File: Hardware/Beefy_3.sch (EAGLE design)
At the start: 21 parts, among them J1 USB-MINIB-5PIN, U1 3.3V, U2 FT232RL-BASICSSOP

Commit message: Added PROD_IDs to library parts and updated them
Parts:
- JP1: device SparkFun:M06SMD-FEMALE-V2 -> SparkFun-Connectors:M06SMD-FEMALE-V2
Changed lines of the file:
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@@
 <grid distance="0.1" unitdist="inch" unit="inch" style="lines" multiple="1" display="no" altdistance="0.01" altunitdist="inch" altunit="inch"/>
 <layers>
-<layer number="1" name="Top" color="4" fill="1" visible="yes" active="no"/>
-<layer number="2" name="Route2" color="1" fill="3" visible="yes" active="no"/>
-<layer number="3" name="Route3" color="4" fill="3" visible="yes" active="no"/>
-<layer number="4" name="Route4" color="1" fill="4" visible="yes" active="no"/>
-<layer number="5" name="Route5" color="4" fill="4" visible="yes" active="no"/>
-<layer number="6" name="Route6" color="1" fill="8" visible="yes" active="no"/>
-<layer number="7" name="Route7" color="4" fill="8" visible="yes" active="no"/>
-<layer number="8" name="Route8" color="1" fill="2" visible="yes" active="no"/>
-<layer number="9" name="Route9" color="4" fill="2" visible="yes" active="no"/>
-<layer number="10" name="Route10" color="1" fill="7" visible="yes" active="no"/>
-<layer number="11" name="Route11" color="4" fill="7" visible="yes" active="no"/>
-<layer number="12" name="Route12" color="1" fill="5" visible="yes" active="no"/>
-<layer number="13" name="Route13" color="4" fill="5" visible="yes" active="no"/>
-<layer number="14" name="Route14" color="1" fill="6" visible="yes" active="no"/>
-<layer number="15" name="Route15" color="4" fill="6" visible="yes" active="no"/>
-<layer number="16" name="Bottom" color="1" fill="1" visible="yes" active="no"/>
-<layer number="17" name="Pads" color="2" fill="1" visible="yes" active="no"/>
-<layer number="18" name="Vias" color="2" fill="1" visible="yes" active="no"/>
-<layer number="19" name="Unrouted" color="6" fill="1" visible="yes" active="no"/>
-<layer number="20" name="Dimension" color="15" fill="1" visible="yes" active="no"/>
-<layer number="21" name="tPlace" color="16" fill="1" visible="yes" active="no"/>
-<layer number="22" name="bPlace" color="14" fill="1" visible="yes" active="no"/>
-<layer number="23" name="tOrigins" color="15" fill="1" visible="yes" active="no"/>
-<layer number="24" name="bOrigins" color="15" fill="1" visible="yes" active="no"/>
-<layer number="25" name="tNames" color="7" fill="1" visible="yes" active="no"/>
-<layer number="26" name="bNames" color="7" fill="1" visible="yes" active="no"/>
-<layer number="27" name="tValues" color="7" fill="1" visible="yes" active="no"/>
-<layer number="28" name="bValues" color="7" fill="1" visible="yes" active="no"/>
+<layer number="1" name="Top" color="4" fill="1" visible="no" active="no"/>
+<layer number="2" name="Route2" color="1" fill="3" visible="no" active="no"/>
+<layer number="3" name="Route3" color="4" fill="3" visible="no" active="no"/>
+<layer number="4" name="Route4" color="1" fill="4" visible="no" active="no"/>
+<layer number="5" name="Route5" color="4" fill="4" visible="no" active="no"/>
+<layer number="6" name="Route6" color="1" fill="8" visible="no" active="no"/>
+<layer number="7" name="Route7" color="4" fill="8" visible="no" active="no"/>
+<layer number="8" name="Route8" color="1" fill="2" visible="no" active="no"/>
+<layer number="9" name="Route9" color="4" fill="2" visible="no" active="no"/>
+<layer number="10" name="Route10" color="1" fill="7" visible="no" active="no"/>
+<layer number="11" name="Route11" color="4" fill="7" visible="no" active="no"/>
+<layer number="12" name="Route12" color="1" fill="5" visible="no" active="no"/>
+<layer number="13" name="Route13" color="4" fill="5" visible="no" active="no"/>
+<layer number="14" name="Route14" color="1" fill="6" visible="no" active="no"/>
+<layer number="15" name="Route15" color="4" fill="6" visible="no" active="no"/>
+<layer number="16" name="Bottom" color="1" fill="1" visible="no" active="no"/>
+<layer number="17" name="Pads" color="2" fill="1" visible="no" active="no"/>
+<layer number="18" name="Vias" color="2" fill="1" visible="no" active="no"/>
+<layer number="19" name="Unrouted" color="6" fill="1" visible="no" active="no"/>
+<layer number="20" name="Dimension" color="15" fill="1" visible="no" active="no"/>
+<layer number="21" name="tPlace" color="16" fill="1" visible="no" active="no"/>
+<layer number="22" name="bPlace" color="14" fill="1" visible="no" active="no"/>
+<layer number="23" name="tOrigins" color="15" fill="1" visible="no" active="no"/>
+<layer number="24" name="bOrigins" color="15" fill="1" visible="no" active="no"/>
+<layer number="25" name="tNames" color="7" fill="1" visible="no" active="no"/>
+<layer number="26" name="bNames" color="7" fill="1" visible="no" active="no"/>
+<layer number="27" name="tValues" color="7" fill="1" visible="no" active="no"/>
+<layer number="28" name="bValues" color="7" fill="1" visible="no" active="no"/>
 <layer number="29" name="tStop" color="7" fill="3" visible="no" active="no"/>
 <layer number="30" name="bStop" color="7" fill="6" visible="no" active="no"/>
@@
 <layer number="35" name="tGlue" color="7" fill="4" visible="no" active="no"/>
 <layer number="36" name="bGlue" color="7" fill="5" visible="no" active="no"/>
-<layer number="37" name="tTest" color="7" fill="1" visible="yes" active="no"/>
-<layer number="38" name="bTest" color="7" fill="1" visible="yes" active="no"/>
+<layer number="37" name="tTest" color="7" fill="1" visible="no" active="no"/>
+<layer number="38" name="bTest" color="7" fill="1" visible="no" active="no"/>
 <layer number="39" name="tKeepout" color="4" fill="11" visible="no" active="no"/>
 <layer number="40" name="bKeepout" color="1" fill="11" visible="no" active="no"/>
@@
 <layer number="44" name="Drills" color="7" fill="1" visible="no" active="no"/>
 <layer number="45" name="Holes" color="7" fill="1" visible="no" active="no"/>
-<layer number="46" name="Milling" color="3" fill="1" visible="yes" active="no"/>
-<layer number="47" name="Measures" color="7" fill="1" visible="yes" active="no"/>
-<layer number="48" name="Document" color="7" fill="1" visible="yes" active="no"/>
-<layer number="49" name="Reference" color="7" fill="1" visible="yes" active="no"/>
-<layer number="50" name="dxf" color="7" fill="1" visible="yes" active="no"/>
-<layer number="51" name="tDocu" color="6" fill="1" visible="yes" active="no"/>
-<layer number="52" name="bDocu" color="7" fill="1" visible="yes" active="no"/>
-<layer number="53" name="tGND_GNDA" color="7" fill="9" visible="yes" active="no"/>
-<layer number="54" name="bGND_GNDA" color="1" fill="9" visible="yes" active="no"/>
-<layer number="56" name="wert" color="7" fill="1" visible="yes" active="no"/>
-<layer number="57" name="tCAD" color="7" fill="1" visible="yes" active="no"/>
-<layer number="59" name="tCarbon" color="7" fill="1" visible="yes" active="no"/>
-<layer number="60" name="bCarbon" color="7" fill="1" visible="yes" active="no"/>
+<layer number="46" name="Milling" color="3" fill="1" visible="no" active="no"/>
+<layer number="47" name="Measures" color="7" fill="1" visible="no" active="no"/>
+<layer number="48" name="Document" color="7" fill="1" visible="no" active="no"/>
+<layer number="49" name="Reference" color="7" fill="1" visible="no" active="no"/>
+<layer number="50" name="dxf" color="7" fill="1" visible="no" active="no"/>
+<layer number="51" name="tDocu" color="6" fill="1" visible="no" active="no"/>
+<layer number="52" name="bDocu" color="7" fill="1" visible="no" active="no"/>
+<layer number="53" name="tGND_GNDA" color="7" fill="9" visible="no" active="no"/>
+<layer number="54" name="bGND_GNDA" color="1" fill="9" visible="no" active="no"/>
+<layer number="56" name="wert" color="7" fill="1" visible="no" active="no"/>
+<layer number="57" name="tCAD" color="7" fill="1" visible="no" active="no"/>
+<layer number="59" name="tCarbon" color="7" fill="1" visible="no" active="no"/>
+<layer number="60" name="bCarbon" color="7" fill="1" visible="no" active="no"/>
 <layer number="90" name="Modules" color="5" fill="1" visible="yes" active="yes"/>
 <layer number="91" name="Nets" color="2" fill="1" visible="yes" active="yes"/>
@@
 <part name="U$1" library="SparkFun" deviceset="5V" device=""/>
 <part name="U$4" library="SparkFun" deviceset="5V" device=""/>
-<part name="JP1" library="SparkFun" deviceset="M06" device="SMD-FEMALE-V2"/>
+<part name="JP1" library="SparkFun-Connectors" deviceset="M06" device="SMD-FEMALE-V2"/>
 <part name="JP3" library="SparkFun" deviceset="FIDUCIAL" device="1X2"/>
 <part name="JP4" library="SparkFun" deviceset="FIDUCIAL" device="1X2"/>

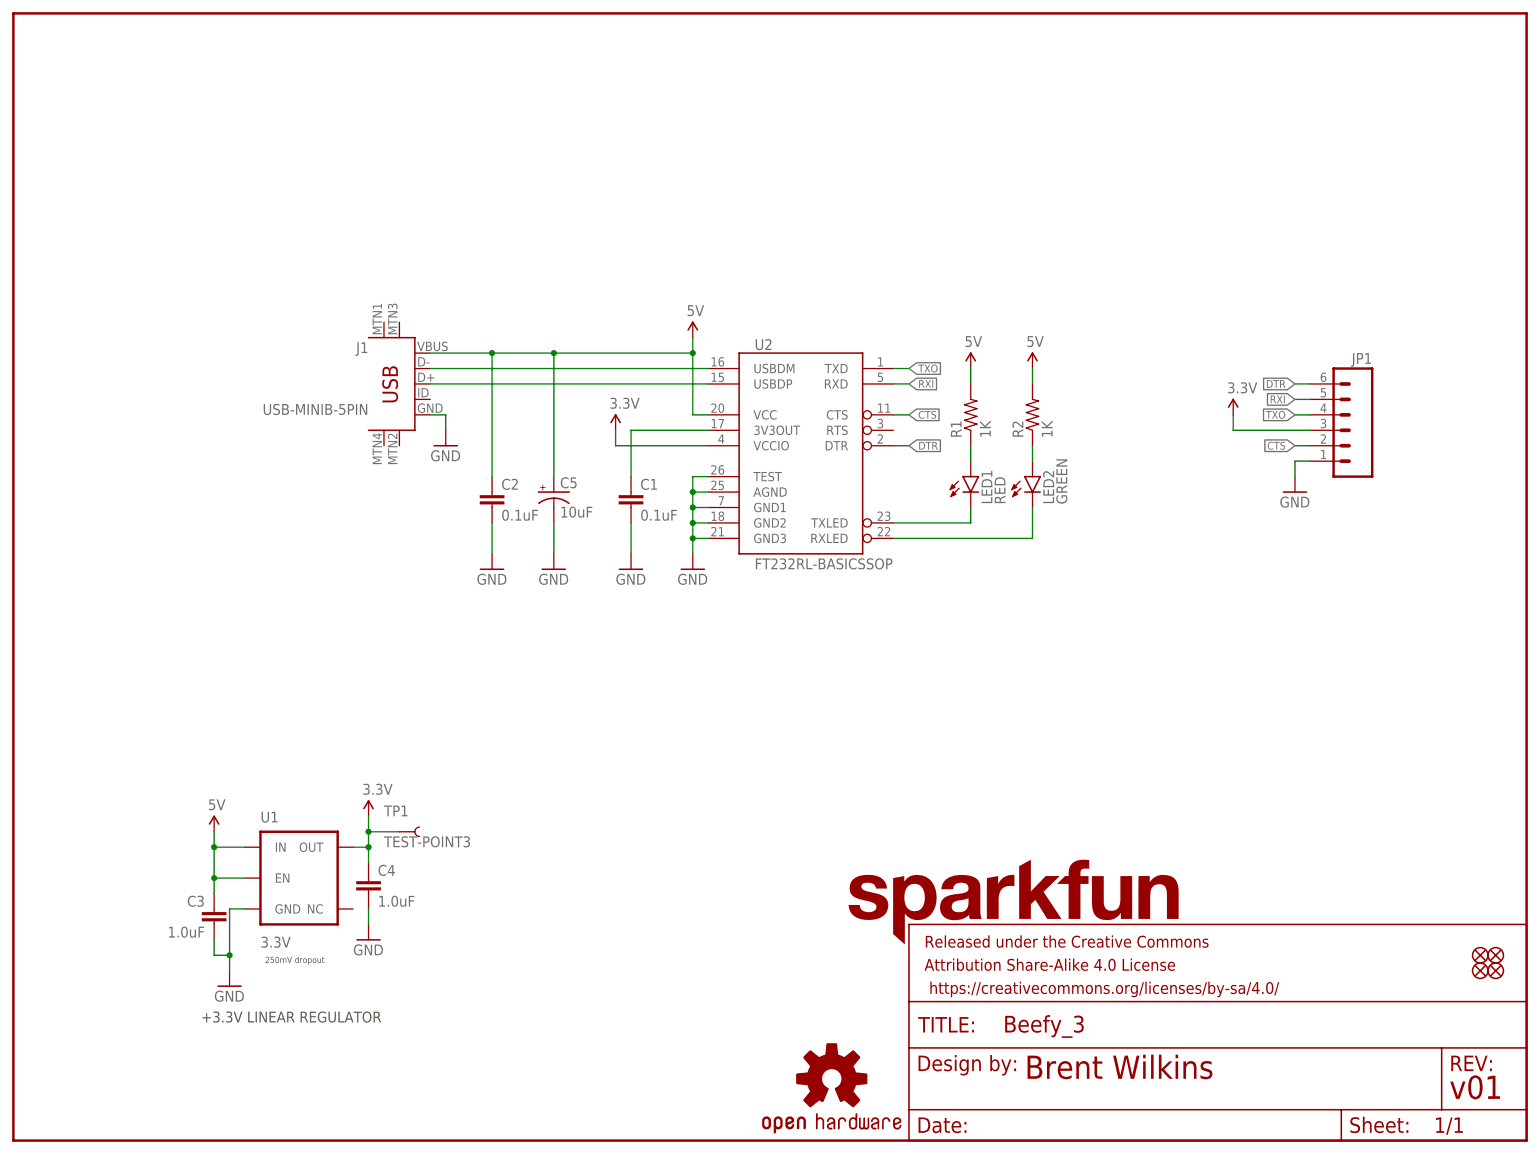
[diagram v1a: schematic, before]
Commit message: First pass at using micro B & FT231X
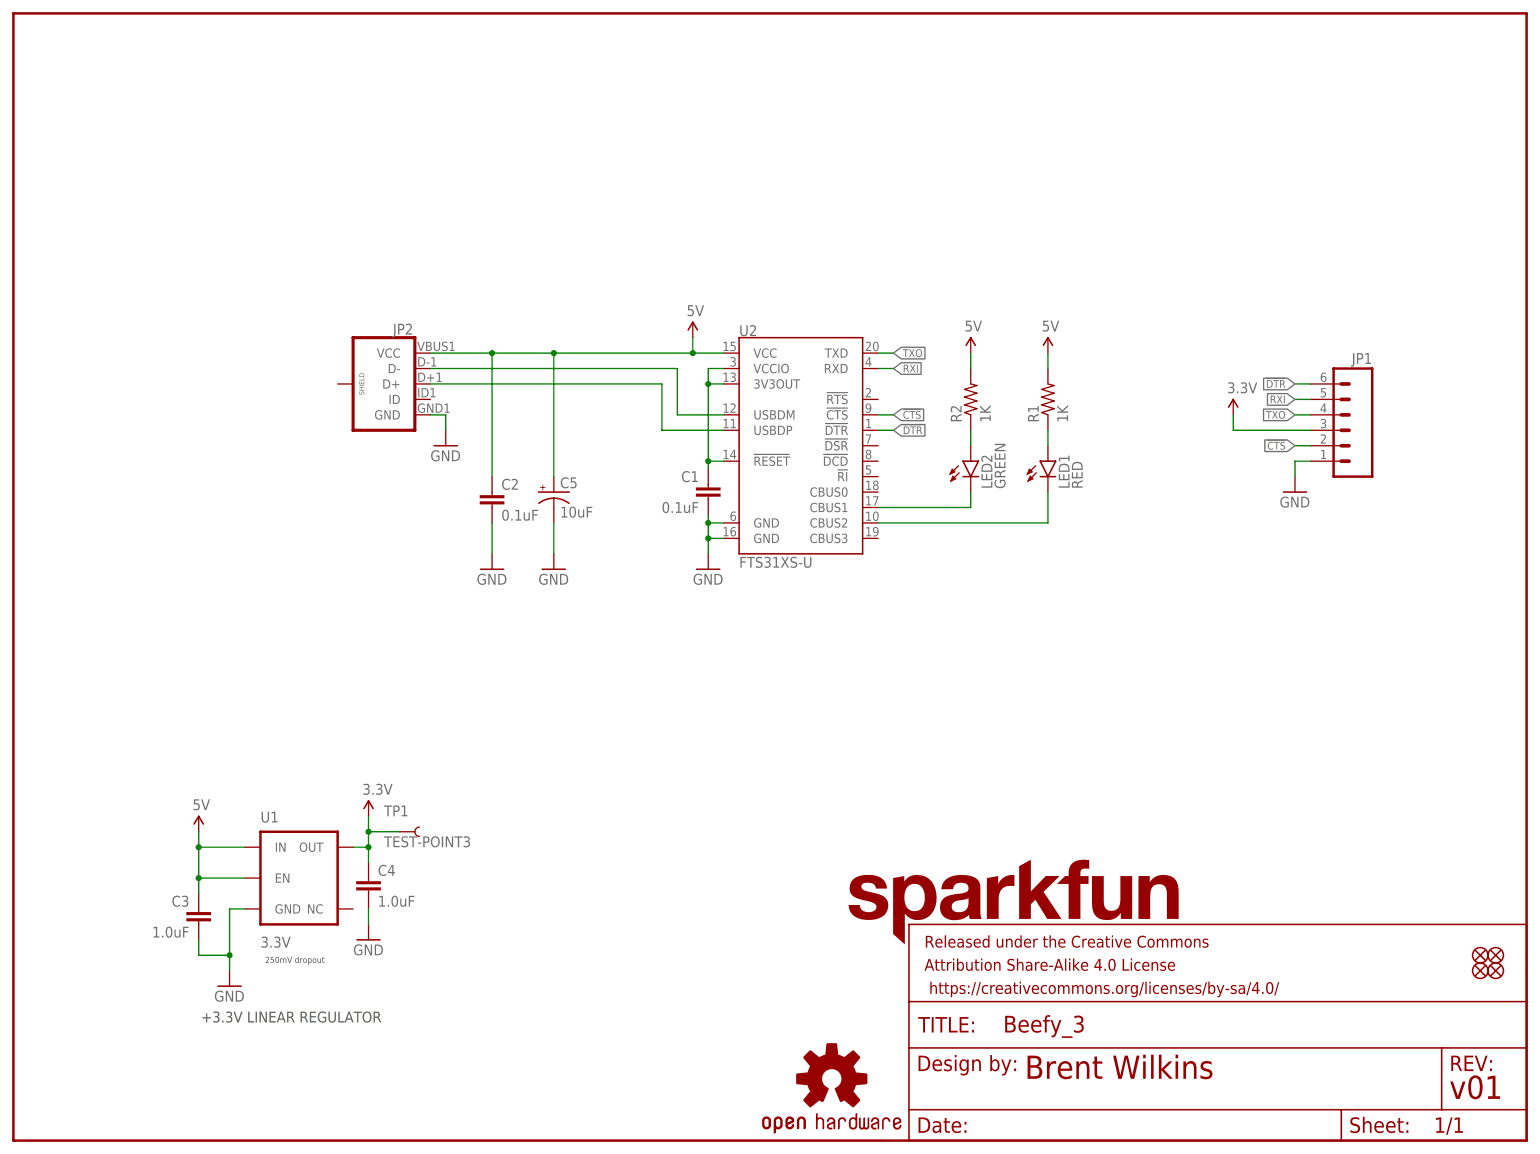
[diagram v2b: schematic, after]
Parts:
- removed J1: USB-MINIB-5PIN, SparkFun-Connectors:USB-MINIB-5PIN
- added JP2: (no value), SparkFun-Connectors:USB_MICROB_PLUGCONN-11752
- U2: value FT232RL-BASICSSOP -> FTS31XS-U; device SparkFun-DigitalIC:FT232RL-BASICSSOP -> SparkFun-DigitalIC:FT231XS
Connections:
- removed net CTS: JP1.2, U2.CTS
- removed net DTR: JP1.6, U2.DTR
- new net !CTS: JP1.2, U2.!CTS
- new net !DTR: JP1.6, U2.!DTR
- new net 3V3LC: C1.1, U2.!RESET, U2.3V3OUT, U2.VCCIO
- net 3.3V: no longer U2.VCCIO
- net 3V3: no longer C1.1, U2.3V3OUT
- net 5V: now also JP2.VCC; no longer J1.VBUS
- net GND: now also JP2.GND, U2.GND@16, U2.GND@6; no longer J1.GND, U2.AGND, U2.GND1, U2.GND2, U2.GND3, U2.TEST
- net RXLED: now also U2.CBUS1; no longer U2.RXLED
- net TXLED: now also U2.CBUS2; no longer U2.TXLED
- net USB_D+: now also JP2.D+; no longer J1.D+
- net USB_D-: now also JP2.D-; no longer J1.D-
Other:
- moved on the sheet: C1, C3, LED1, LED2, R1, R2

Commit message: New layout
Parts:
- removed TP1: TEST-POINT3, SparkFun-Passives:TEST-POINT3
- C1, C2: value 0.1uF -> 1.0uF; device SparkFun-Capacitors:0.1UF-25V(+80/-20%)(0603) -> SparkFun-Capacitors:1.0UF-16V-10%(0603)
- C3: value 1.0uF -> 0.1uF; device SparkFun-Capacitors:1.0UF-16V-10%(0603) -> SparkFun-Capacitors:0.1UF-25V(+80/-20%)(0603)
- C4: value 1.0uF -> 10uF; device SparkFun-Capacitors:1.0UF-16V-10%(0603) -> SparkFun-Capacitors:10UF-16V-10%(TANT)
- C5: value 10uF -> 0.1uF; device SparkFun-Capacitors:10UF-16V-10%(TANT) -> SparkFun-Capacitors:0.1UF-25V(+80/-20%)(0603)
- JP1: device SparkFun-Connectors:M06SMD-FEMALE-V2 -> SparkFun-Connectors:USB_MICROB_PLUGCONN-11752
- JP2: device SparkFun-Connectors:USB_MICROB_PLUGCONN-11752 -> SparkFun-Connectors:M06SMD-FEMALE-V2
- renumbered FRAME2 to FRAME1, LED1 to D2, LED2 to D1, U$2 to LOGO2
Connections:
- removed net 3.3V: JP1.3
- net !CTS: now also JP2.2; no longer JP1.2
- net !DTR: now also JP2.6; no longer JP1.6
- net 3V3: now also C2.1, JP2.3; no longer C4.1, TP1.1
- net 3V3LC: now also C5.1; no longer C1.1
- net 5V: now also C1.1, C4.+, JP1.VCC; no longer C2.1, C5.+, JP2.VCC
- net GND: now also C4.-, C5.2, JP1.GND, JP2.1; no longer C4.2, C5.-, JP1.1, JP2.GND
- net N$1: now also R2.1; no longer R1.1
- net N$2: now also R1.1; no longer R2.1
- net RXI: now also JP2.5; no longer JP1.5
- net TXO: now also JP2.4; no longer JP1.4
- net USB_D+: now also JP1.D+; no longer JP2.D+
- net USB_D-: now also JP1.D-; no longer JP2.D-
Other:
- note added: "THIS PCBA IS DESIGNED FOR +3.3V"
- moved on the sheet: C1, C2, C3, R1, R2, U1
